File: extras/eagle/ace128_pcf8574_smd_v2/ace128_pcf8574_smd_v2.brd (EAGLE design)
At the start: 30.5 x 30.5 mm, 13 parts, among them J1 GROVE I2C, U1 PCF8574T

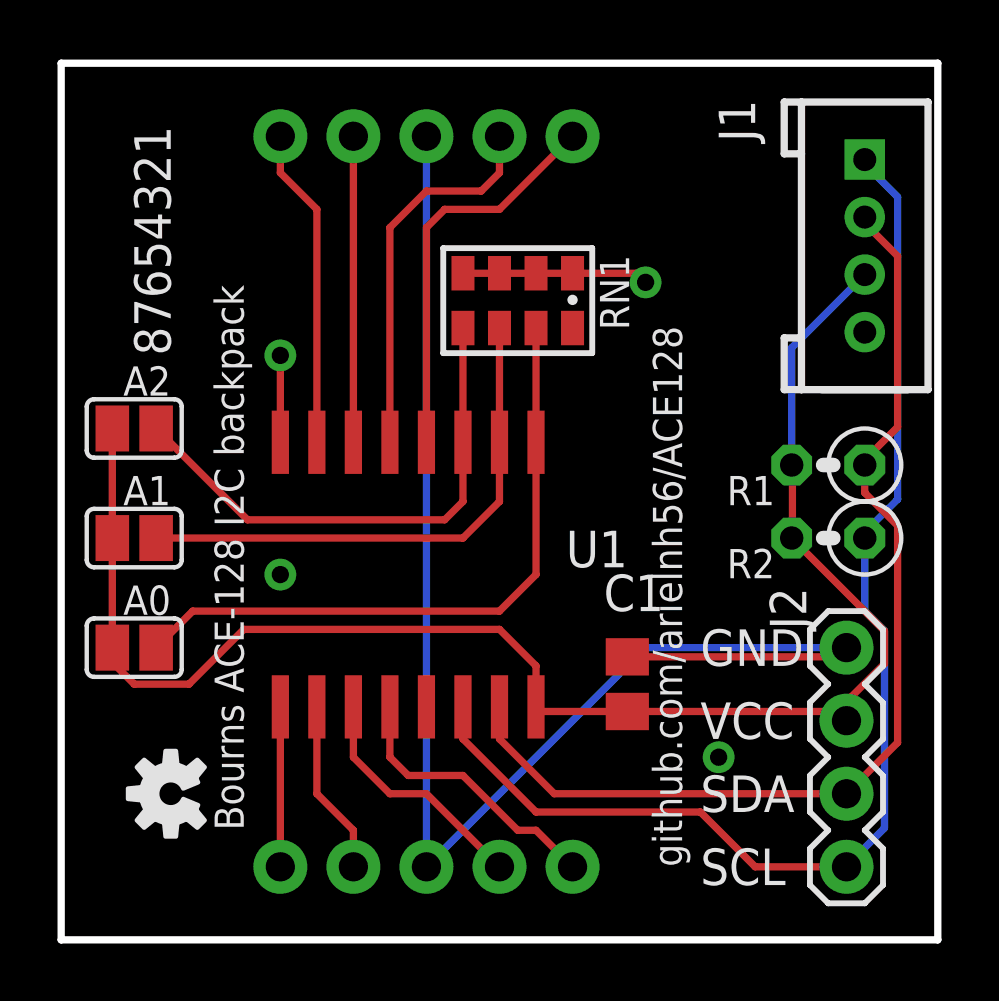
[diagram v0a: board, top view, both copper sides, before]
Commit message: v2.1 board
change c1 to 0603
add c2 10uf 0805
route tidying
silkscreen adds for version and address ranges.
general silkscreen shuffle
tented vias
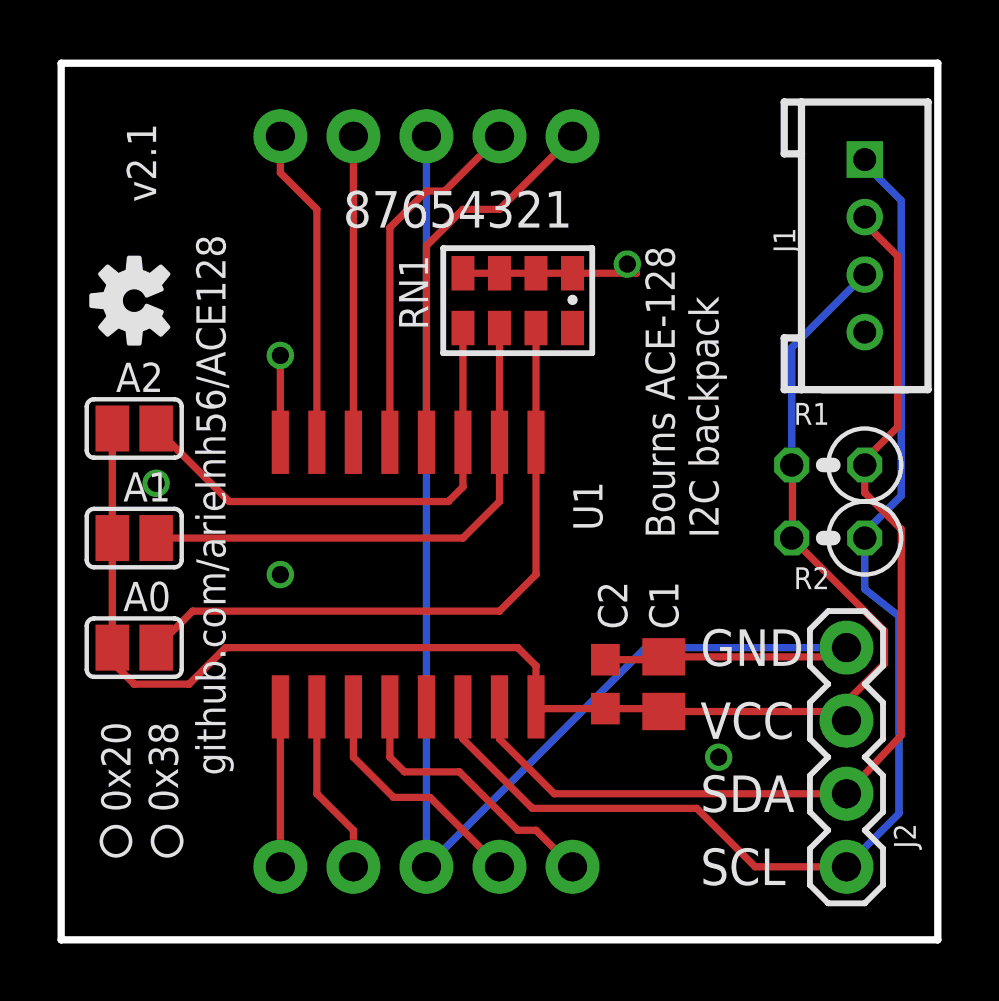
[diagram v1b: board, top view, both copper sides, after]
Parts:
- added C2: 10uF, rcl:C0805
- C1: device rcl:C0805 -> rcl:C0603
- moved LOGO1 17.2 mm to (2.54, 22.2)
- moved C1 0.76 mm to (18.9, 8.89)
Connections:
- net GND: now also C2.2
- net VCC: now also C2.1
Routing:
- net N$3: track 18.3 -> 17.5 mm
- net GND: track 60.4 -> 61.2 mm, vias 4 -> 5
- net P1: track 13.3 -> 12.6 mm
- net SCL: track 42.7 -> 43.3 mm
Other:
- board text added: "0x20"
- board text added: "0x38"
- board text added: "v2.1"
